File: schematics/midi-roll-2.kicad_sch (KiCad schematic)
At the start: 21 parts, among them M1 Stepper_Motor_unipolar_5pin, SW1 SW_Push_SPDT, SW10 SW_Push_SPDT, SW11 SW_Push_SPDT, SW12 SW_Push_SPDT, SW13 SW_Push_SPDT, SW14 SW_Push_SPDT, SW15 SW_Push_SPDT, SW16 SW_Push_SPDT, SW2 SW_Push_SPDT, SW3 SW_Push_SPDT, SW4 SW_Push_SPDT, SW5 SW_Push_SPDT, SW6 SW_Push_SPDT, SW7 SW_Push_SPDT, SW8 SW_Push_SPDT, SW9 SW_Push_SPDT, U1 WeMos_D1_mini, U2 CD4051B, U3 CD4051B, U4 ULN2003A

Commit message: updated schematic
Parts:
- added C1: C, symbol Device:C
- added R1, R10, R11, R2, R3, R4, R5, R6, R7, R8, R9: 1K, symbol Device:R
- added R12: 10K, symbol Device:R
- added SW17: SW_Push, symbol Switch:SW_Push
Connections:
- net +5V: now also C1.1, R2.1, SW17.1
- net GND: now also U2.7 (VEE), U3.7 (VEE), C1.2, R1.1, R10.1, R11.1, R12.2, R3.1, R4.1, R5.1, R6.1, R7.1, R8.1, R9.1
- net SW3: now reaches SW3.2 (B), U2.15 (X2)
- net SW3: now also R6.2
- net at SW13.2 (B): no longer U3.1 (X4)
- net B: now reaches U2.10 (B), U3.10 (B)
- net B: now also U1.11 (D4), R2.2; no longer U1.13 (SDA/D2)
- net A: now reaches U2.11 (A), U3.11 (A)
- net A: now also U1.3 (D0), R1.2; no longer U1.14 (SCL/D1)
- net at SW12.2 (B): no longer U3.12 (X3)
- net at SW9.2 (B): no longer U3.13 (X0)
- net at SW10.2 (B): no longer U3.14 (X1)
- net at SW11.2 (B): no longer U3.15 (X2)
- net at SW15.2 (B): no longer U3.2 (X6)
- net IN4: now reaches U1.6 (MOSI/D7)
- net IN4: now also U4.4 (I4); no longer U3.3 (X)
- net at SW16.2 (B): no longer U3.4 (X7)
- net at SW14.2 (B): no longer U3.5 (X5)
- net C: now reaches U2.9 (C), U3.9 (C)
- net C: now also U1.12 (D3); no longer U1.4 (SCK/D5)
- net SW4: now reaches SW4.2 (B), U2.12 (X3)
- net SW4: now also R7.2
- net ORANGE: now reaches M1.2
- net ORANGE: now also U4.13 (O4)
- net PINK: now reaches M1.3 (-)
- net PINK: now also U4.15 (O2)
- net YELLOW: now reaches M1.4
- net YELLOW: now also U4.14 (O3)
- net BLUE: now reaches M1.5
- net BLUE: now also U4.16 (O1)
- net IN1: now reaches U4.1 (I1)
- net IN1: now also U1.4 (SCK/D5)
- net IN2: now reaches U4.2 (I2)
- net IN2: now also U1.5 (MISO/D6)
- net IN3: now reaches U4.3 (I3)
- net IN3: now also U1.7 (CS/D8), R3.2
- net SW7: now reaches SW7.2 (B), U2.2 (X6)
- net SW7: now also R10.2
- net SW2: now reaches SW2.2 (B), U2.14 (X1)
- net SW2: now also R5.2
- net SW5: now reaches SW5.2 (B), U2.1 (X4)
- net SW5: now also R8.2
- net SW8: now reaches SW8.2 (B), U2.4 (X7)
- net SW8: now also R11.2
- net SW1: now reaches SW1.2 (B), U2.13 (X0)
- net SW1: now also R12.1, R4.2, SW17.2
- net MUX1COM: now reaches U2.3 (X)
- net MUX1COM: now also U1.14 (SCL/D1); no longer U1.5 (MISO/D6)
- net SW6: now reaches SW6.2 (B), U2.5 (X5)
- net SW6: now also R9.2
- new net MUX2COM: U1.13 (SDA/D2), U3.3 (X)
- new net SW10: U3.14 (X1)
- new net SW11: U3.15 (X2)
- new net SW12: U3.12 (X3)
- new net SW13: U3.1 (X4)
- new net SW14: U3.5 (X5)
- new net SW15: U3.2 (X6)
- new net SW16: U3.4 (X7)
- new net SW9: U3.13 (X0)
- no-connect marks 0 -> 11
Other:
- note added: "MICROCONTROLLER"
- note added: "MOTOR CONTROLLER"
- note added: "MULTIPLEXERS"
- note added: "SWITCHES"
- note added: "TODO power en ground and pulldown of switched...need to be checken with propper microswitch"
- note added: "mux one"
- note added: "mux two"
- note added: "this is how my pushbuttons are connected"
- moved on the sheet: M1, SW1, SW10, SW11, SW12, SW13, SW14, SW15, SW16, SW2, SW3, SW4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

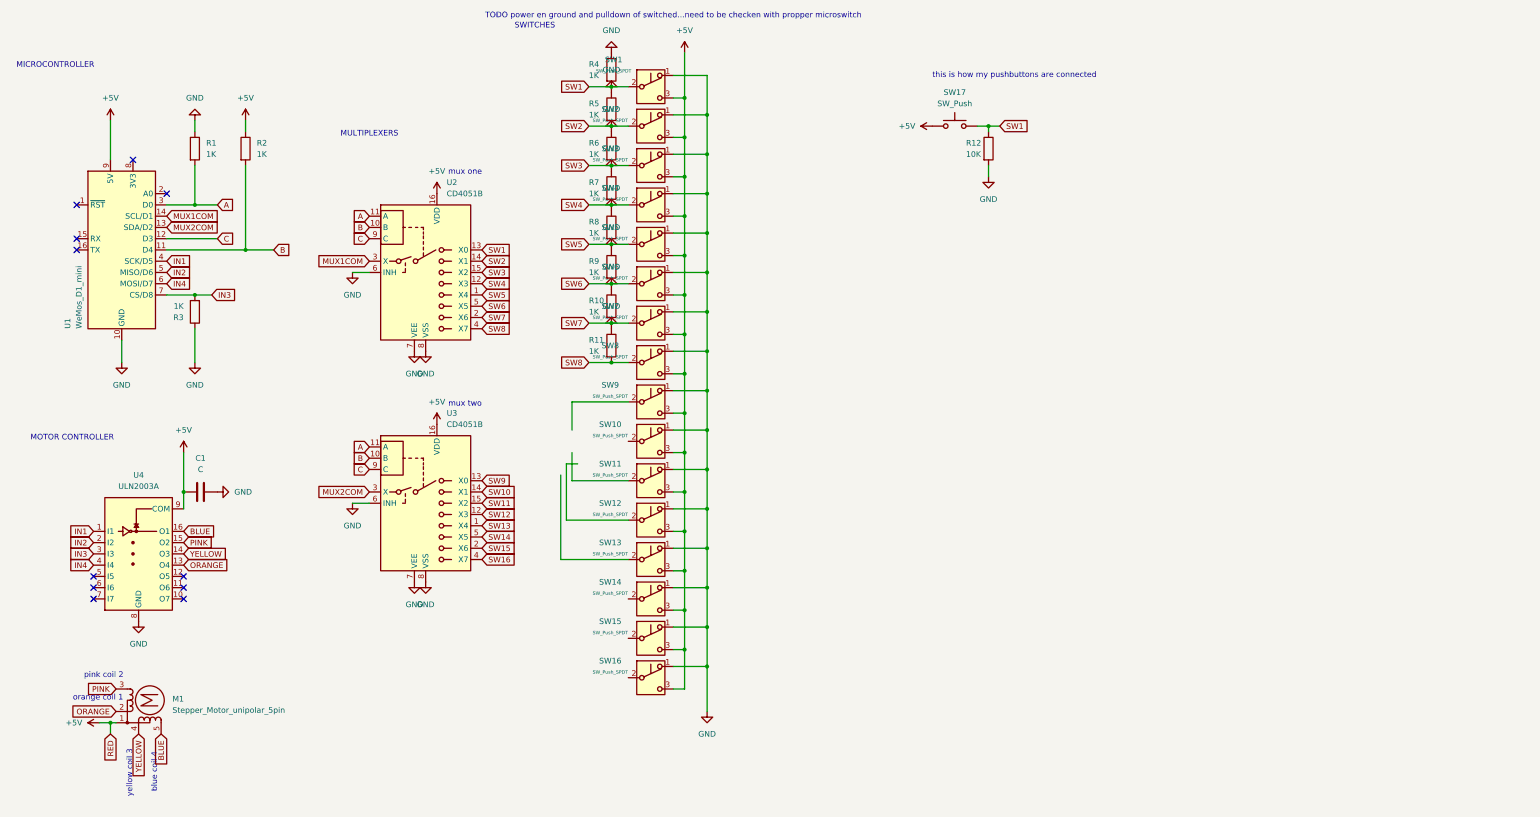
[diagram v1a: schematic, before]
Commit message: added 2 more motors and controllers
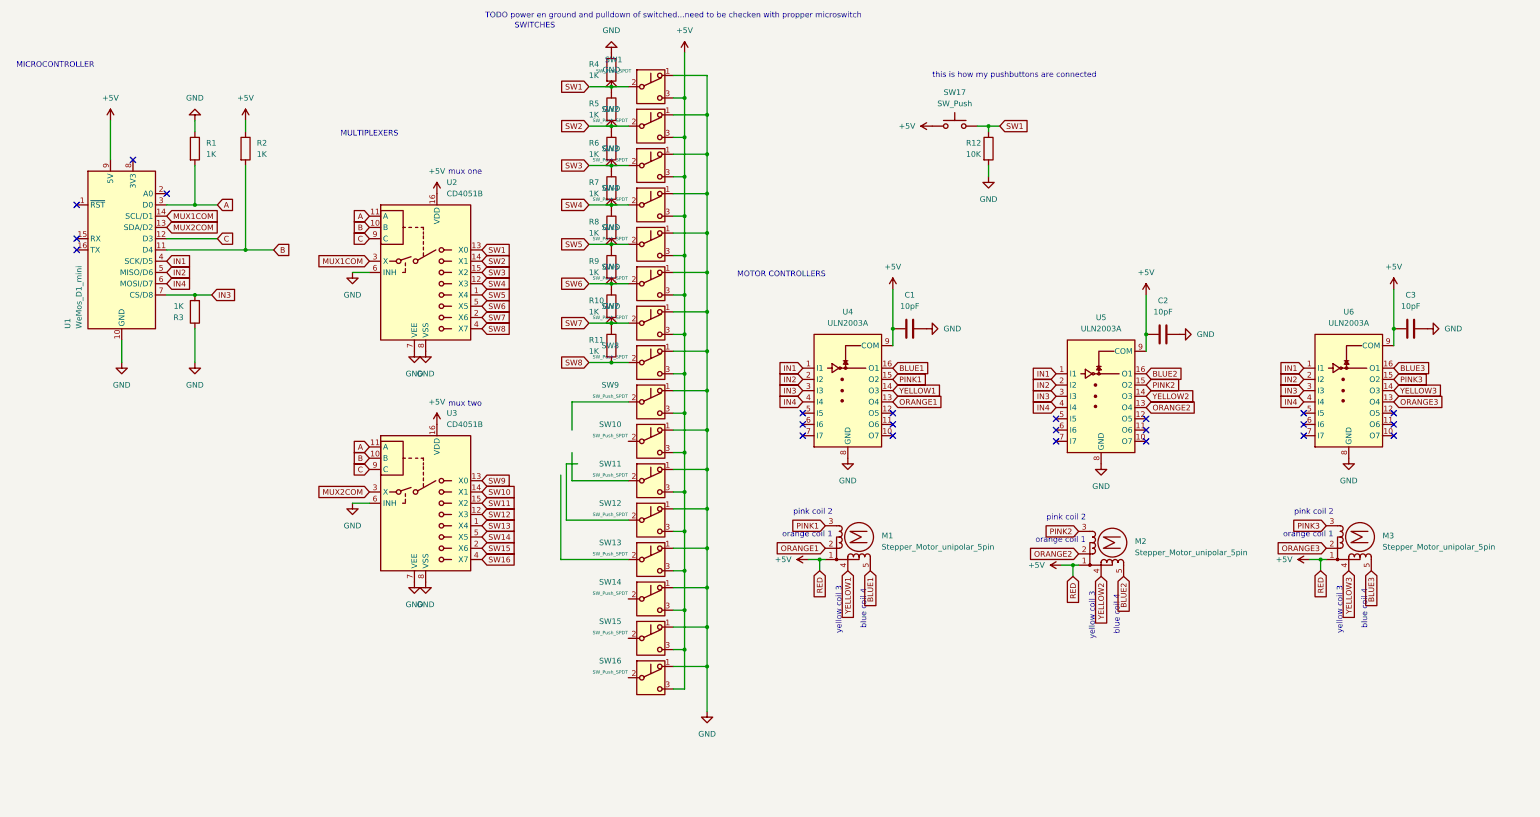
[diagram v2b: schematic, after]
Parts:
- added C2, C3: 10pF, symbol Device:C
- added M2, M3: Stepper_Motor_unipolar_5pin, symbol Motor:Stepper_Motor_unipolar_5pin
- added U5, U6: ULN2003A, symbol Transistor_Array:ULN2003A
- C1: value C -> 10pF
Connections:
- net +5V: now also C2.1, C3.1, M2.1, M3.1, U5.9 (COM), U6.9 (COM)
- net GND: now also C2.2, C3.2, U5.8 (GND), U6.8 (GND)
- net IN1: now also U5.1 (I1), U6.1 (I1)
- net IN2: now also U5.2 (I2), U6.2 (I2)
- net IN3: now also U5.3 (I3), U6.3 (I3)
- net IN4: now also U5.4 (I4), U6.4 (I4)
- net BLUE renamed BLUE1
- net ORANGE renamed ORANGE1
- net PINK renamed PINK1
- net YELLOW renamed YELLOW1
- new net BLUE2: M2.5, U5.16 (O1)
- new net BLUE3: M3.5, U6.16 (O1)
- new net ORANGE2: M2.2, U5.13 (O4)
- new net ORANGE3: M3.2, U6.13 (O4)
- new net PINK2: M2.3 (-), U5.15 (O2)
- new net PINK3: M3.3 (-), U6.15 (O2)
- new net YELLOW2: M2.4, U5.14 (O3)
- new net YELLOW3: M3.4, U6.14 (O3)
- no-connect marks 11 -> 23
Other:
- note added: "MOTOR CONTROLLERS"
- note removed: "MOTOR CONTROLLER"
- moved on the sheet: C1, M1, U4
